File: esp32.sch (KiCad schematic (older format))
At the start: 4 parts, among them SW62 SW_Push, SW63 SW_Push, U4 Micro-32-HS-Wismar

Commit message: Layout fortgesetzt
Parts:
- added D55: LED_Small, LED_THT:LED_D3.0mm_Horizontal_O1.27mm_Z2.0mm, symbol Device:LED_Small
- added R11: 470, Resistor_SMD:R_0603_1608Metric_Pad0.98x0.95mm_HandSolder, symbol Device:R_Small
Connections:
- net GND: now also D55.1 (K)
- net at U4.24 (IO2): no longer SW63.1
- net at U4.25 (IO0): now also SW63.1
- net at U4.36 (IO22): now also R11.2
- new net: D55.2 (A), R11.1
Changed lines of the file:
@@
 Wire Wire Line
 	3300 2650 4050 2650
-Text HLabel 6700 2750 2    50   Output ~ 0
-TX_out
-Text HLabel 6700 2850 2    50   Input ~ 0
-RX_in
-Wire Wire Line
-	6700 2850 6000 2850
-Wire Wire Line
-	6000 2750 6700 2750
 $Comp
 L Switch:SW_Push SW62
@@
 Wire Wire Line
 	4050 2650 4500 2650
-Wire Wire Line
-	6550 4000 6550 3850
-Wire Wire Line
-	6550 3850 6000 3850
 $Comp
 L power:GND #PWR0129
@@
 Wire Wire Line
 	4050 4400 4050 4500
+Wire Wire Line
+	6000 3750 6550 3750
+Wire Wire Line
+	6550 3750 6550 4000
+$Comp
+L power:GND #PWR033
+U 1 1 60FDD502
+P 7250 4550
+F 0 "#PWR033" H 7250 4300 50  0001 C CNN
+F 1 "GND" H 7255 4377 50  0000 C CNN
+F 2 "" H 7250 4550 50  0001 C CNN
+F 3 "" H 7250 4550 50  0001 C CNN
+	1    7250 4550
+	1    0    0    -1
+$EndComp
+$Comp
+L Device:R_Small R11
+U 1 1 60FDDAD5
+P 6700 2650
+F 0 "R11" V 6504 2650 50  0000 C CNN
+F 1 "470" V 6595 2650 50  0000 C CNN
+F 2 "Resistor_SMD:R_0603_1608Metric_Pad0.98x0.95mm_HandSolder" H 6700 2650 50  0001 C CNN
+F 3 "~" H 6700 2650 50  0001 C CNN
+	1    6700 2650
+	0    1    1    0
+$EndComp
+Wire Wire Line
+	6000 2750 7550 2750
+Wire Wire Line
+	7550 2850 6000 2850
+Text HLabel 7550 2850 2    50   Input ~ 0
+RX_in
+Text HLabel 7550 2750 2    50   Output ~ 0
+TX_out
+$Comp
+L Device:LED_Small D55
+U 1 1 60FE43BF
+P 7250 3450
+F 0 "D55" V 7296 3380 50  0000 R CNN
+F 1 "LED_Small" V 7205 3380 50  0000 R CNN
+F 2 "LED_THT:LED_D3.0mm_Horizontal_O1.27mm_Z2.0mm" V 7250 3450 50  0001 C CNN
+F 3 "~" V 7250 3450 50  0001 C CNN
+	1    7250 3450
+	0    -1   -1   0
+$EndComp
+Wire Wire Line
+	6000 2650 6600 2650
+Wire Wire Line
+	6800 2650 7250 2650
+Wire Wire Line
+	7250 2650 7250 3350
+Wire Wire Line
+	7250 3550 7250 4550
 $EndSCHEMATC

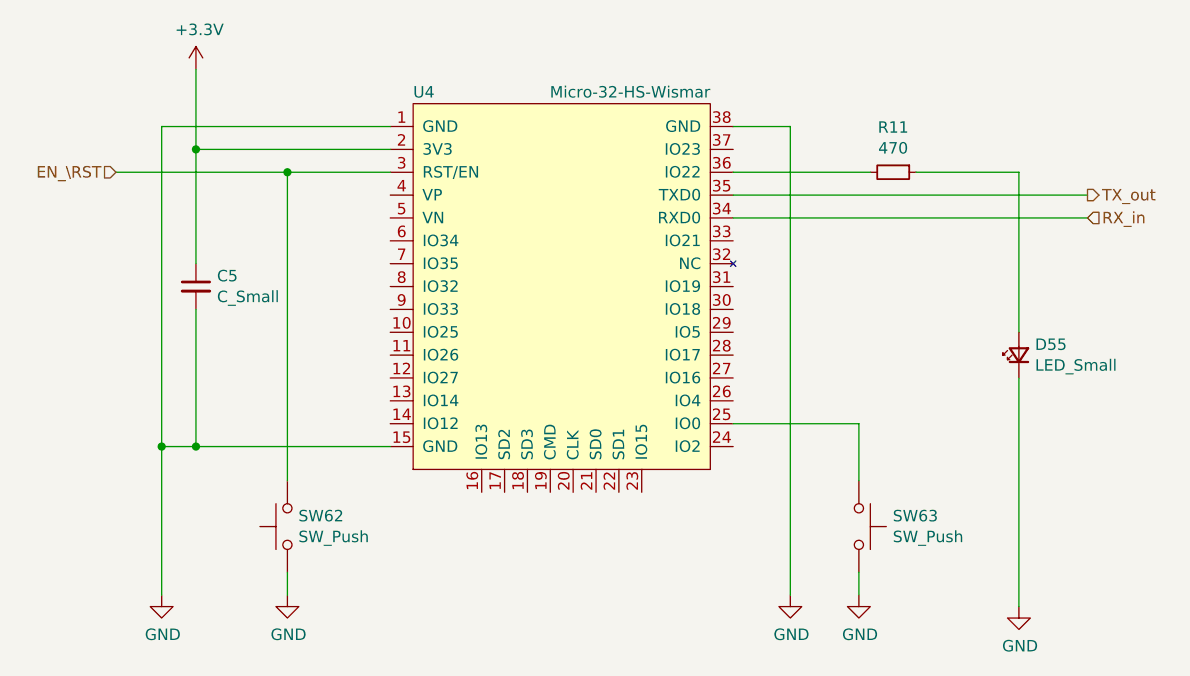
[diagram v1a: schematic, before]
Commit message: Layout sent to JLCPCB
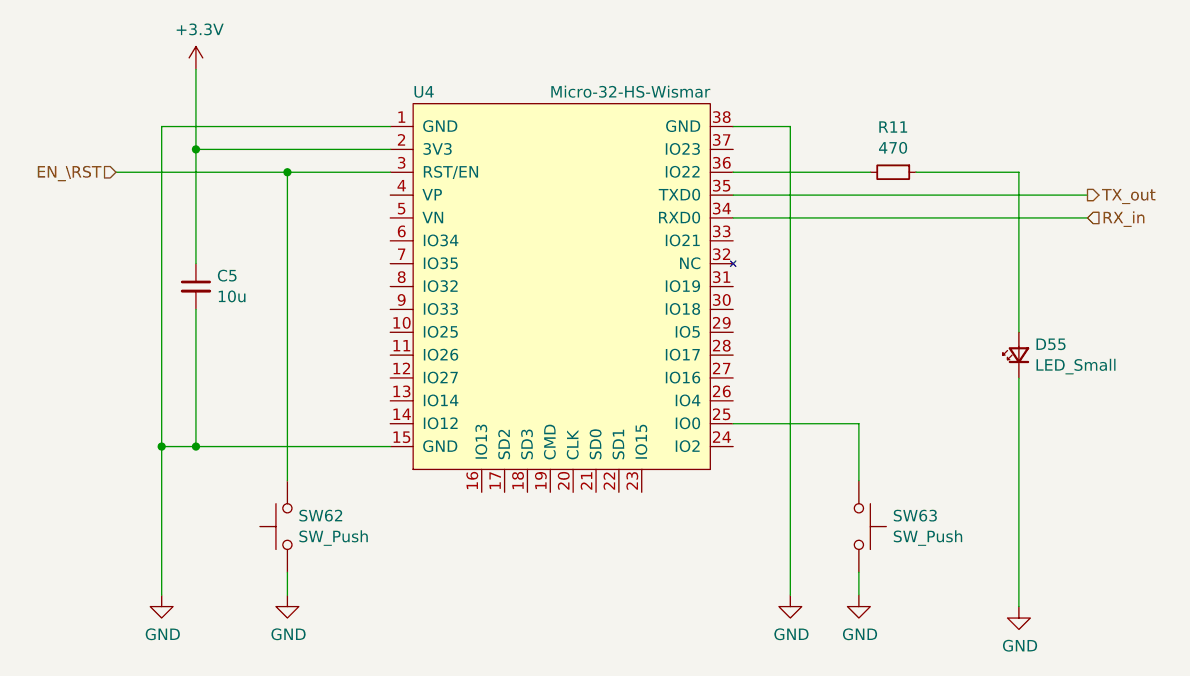
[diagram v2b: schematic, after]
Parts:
- C5: value C_Small -> 10u; footprint Capacitor_SMD:C_0603_1608Metric -> Capacitor_SMD:C_1206_3216Metric_Pad1.33x1.80mm_HandSolder
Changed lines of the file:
@@
 P 3650 3150
 F 0 "C5" H 3742 3196 50  0000 L CNN
-F 1 "C_Small" H 3742 3105 50  0000 L CNN
-F 2 "Capacitor_SMD:C_0603_1608Metric" H 3650 3150 50  0001 C CNN
+F 1 "10u" H 3742 3105 50  0000 L CNN
+F 2 "Capacitor_SMD:C_1206_3216Metric_Pad1.33x1.80mm_HandSolder" H 3650 3150 50  0001 C CNN
 F 3 "~" H 3650 3150 50  0001 C CNN
 	1    3650 3150

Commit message: Filterung in den USB-Leitungen, VBus besser abgeblockt, Enter Taste gedreht
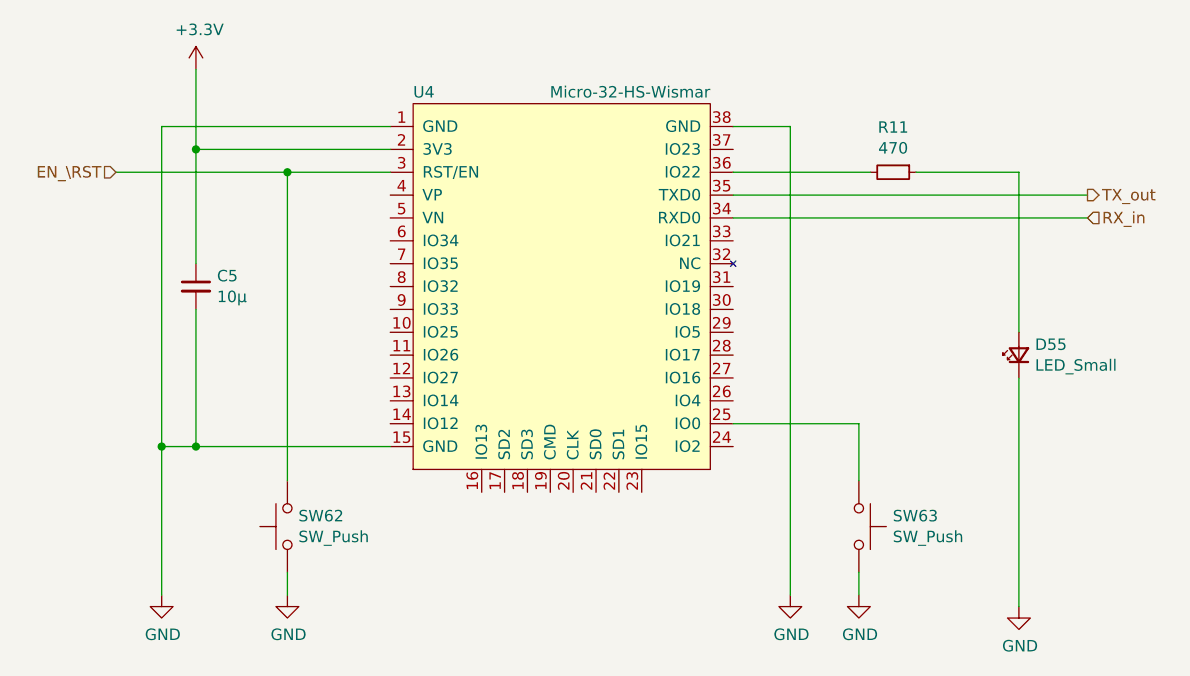
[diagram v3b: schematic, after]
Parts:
- C5: value 10u -> 10μ
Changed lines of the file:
@@
 P 3650 3150
 F 0 "C5" H 3742 3196 50  0000 L CNN
-F 1 "10u" H 3742 3105 50  0000 L CNN
+F 1 "10μ" H 3742 3105 50  0000 L CNN
 F 2 "Capacitor_SMD:C_1206_3216Metric_Pad1.33x1.80mm_HandSolder" H 3650 3150 50  0001 C CNN
 F 3 "~" H 3650 3150 50  0001 C CNN
